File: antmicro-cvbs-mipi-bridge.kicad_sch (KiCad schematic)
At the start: 105 parts, among them IC1 ADV7280BCPZ-M, IC2 TLV70018, IC4 SN74AUP1G17DCKR, IC5 SN74AUP1G17DCKR, J1 WE_68715014522, J2 61300211121, J7 61300211121, Q1 BSS138APW, Q2 BSS138APW, Q3 BSS138APW, Q4 BSS138APW, Y1 ABM8G-28.63636MHZ-18-D2Y-T

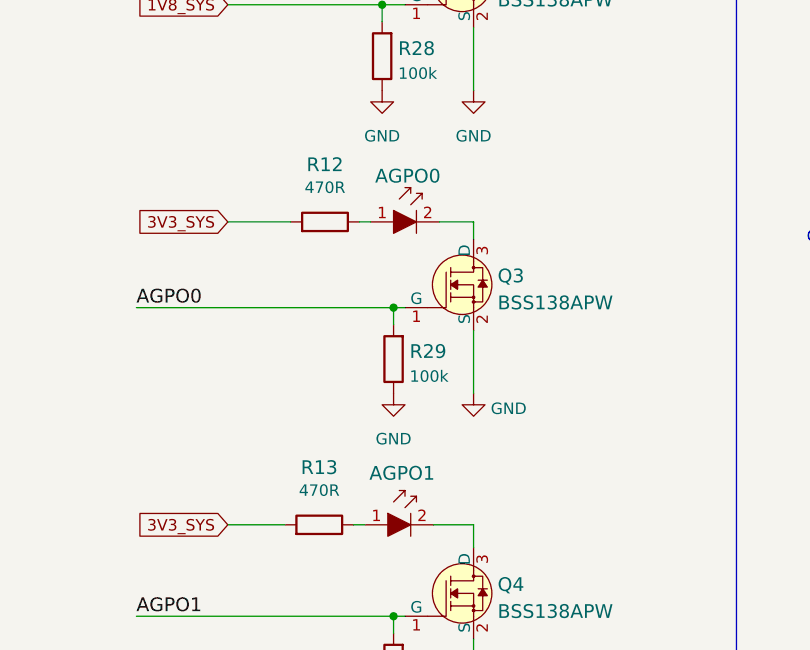
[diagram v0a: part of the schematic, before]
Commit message: Corrected ADV7280 footprint. Finished corrections and optimizations. Added missing step model
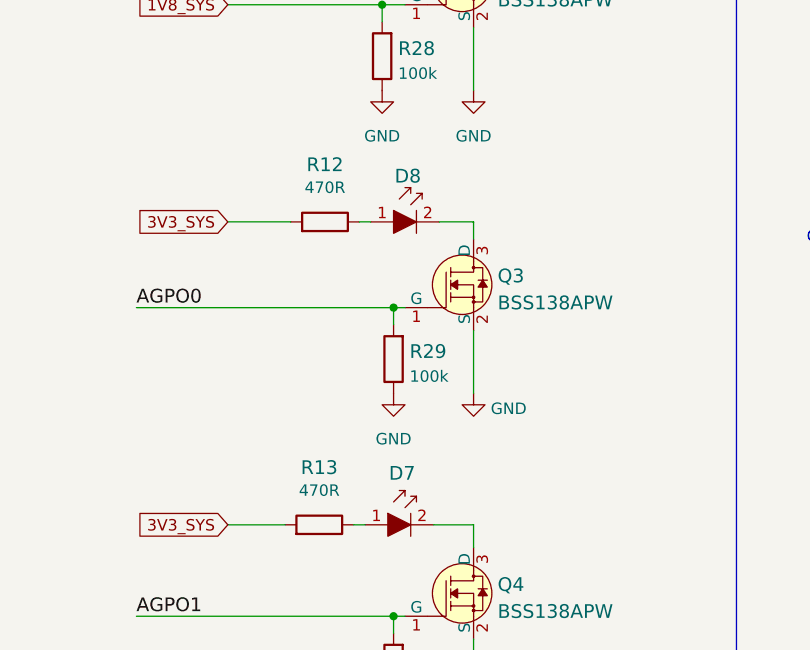
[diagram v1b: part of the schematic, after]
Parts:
- renumbered AGPO1 to D7, AGPO0 to D8
